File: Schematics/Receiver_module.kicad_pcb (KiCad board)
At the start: 2 copper layers, 54.6 x 44.5 mm, 17 parts, among them J1 I2C_ToTagger, T1 BC237, T2 BC237, T3 BC237

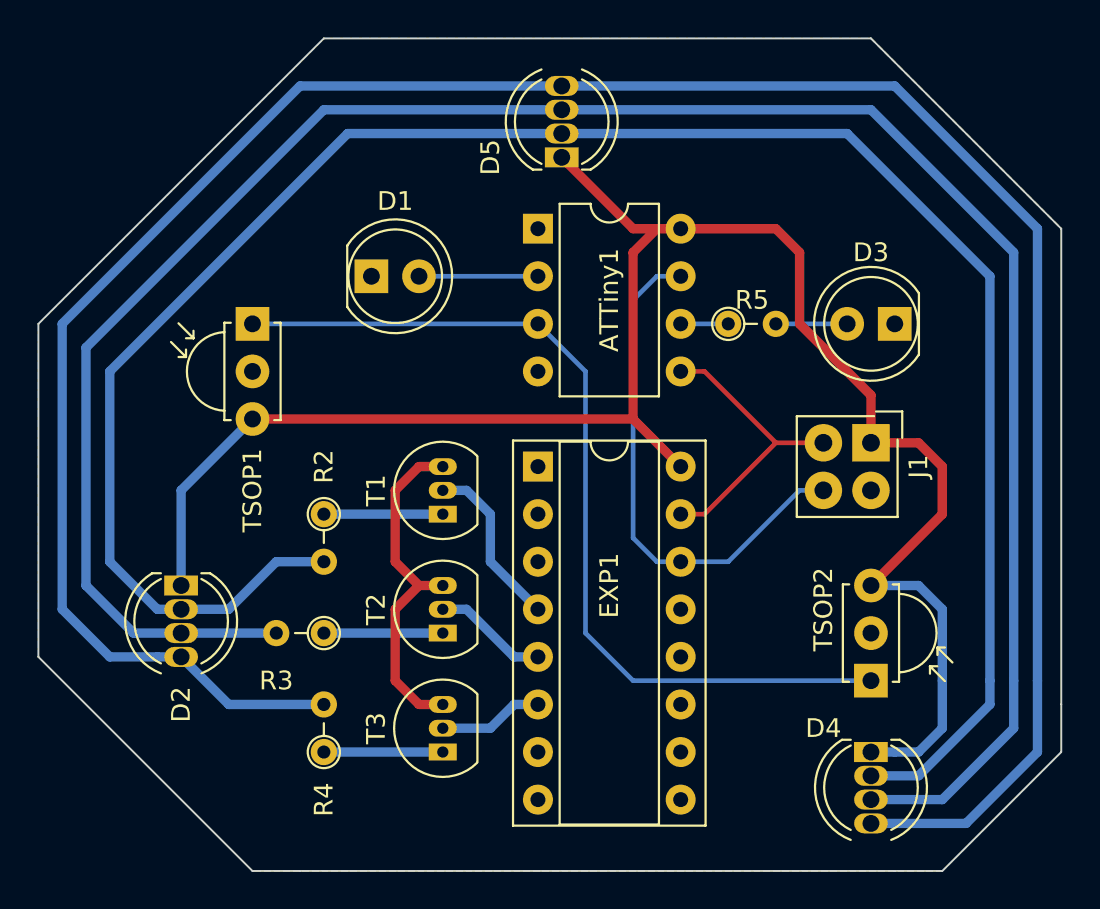
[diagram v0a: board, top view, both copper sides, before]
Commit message: New Version of Tagger/Receiver Schematics and PCBs
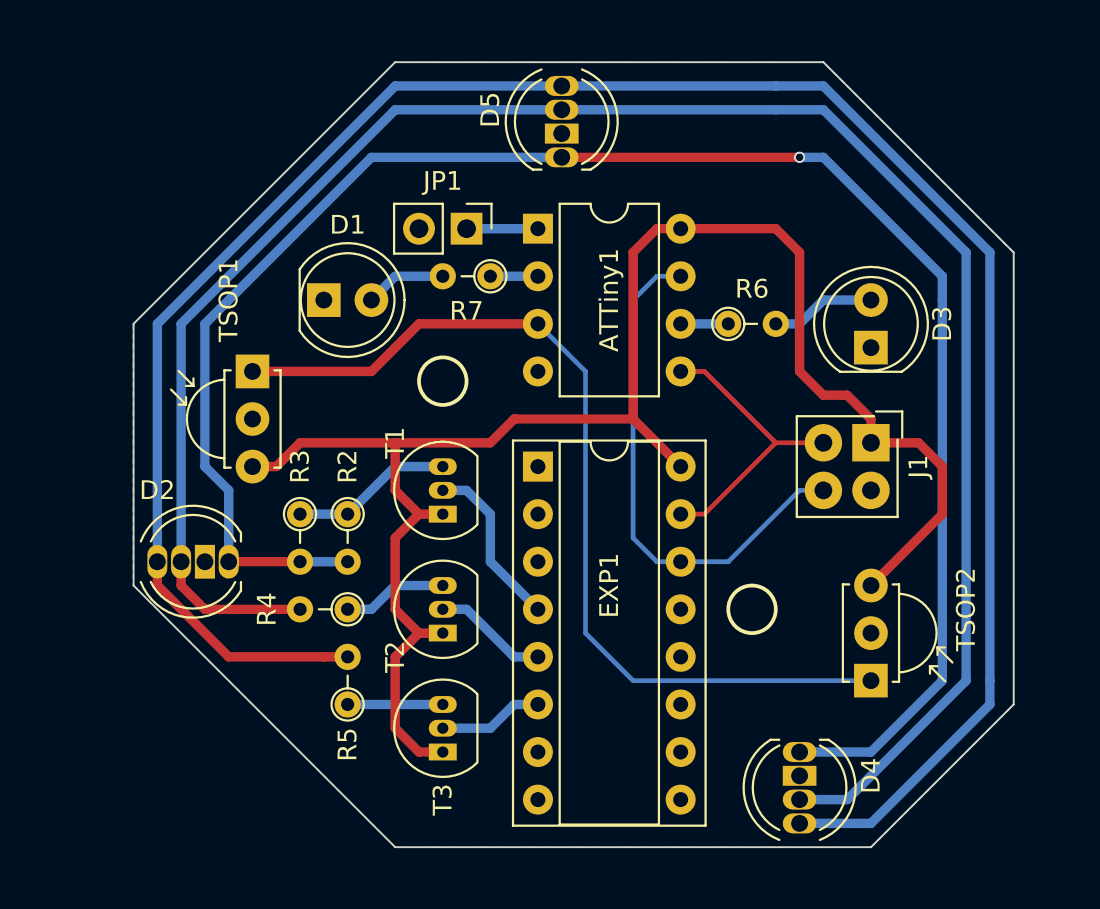
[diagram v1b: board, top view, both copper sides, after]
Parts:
- added JP1: Jumper_NO_Small, Pin_Headers:Pin_Header_Straight_1x02_Pitch2.54mm, F.Cu at (99.1, 94.0)
- added R6: R6, Resistors_THT:R_Axial_DIN0204_L3.6mm_D1.6mm_P2.54mm_Vertical, F.Cu at (113.0, 99.1)
- added R7: R, Resistors_THT:R_Axial_DIN0204_L3.6mm_D1.6mm_P2.54mm_Vertical, F.Cu at (100.3, 96.5)
- D2, D4, D5: value LED_ARGB -> LED_CRGB; footprint LEDs:LED_D5.0mm-4 -> RGB_LED_CC_5mm:LED_D5.0mm-4
- R2: value R2 -> 150R
- R3: value R3 -> 150R
- R4: value R4 -> 1k5
- R5: value R5 -> 1k
- moved R5 28.7 mm to (92.7, 119.4), turned to 90 degrees
- moved R4 7.73 mm to (92.7, 114.3), turned to 180 degrees
- moved R3 6.48 mm to (90.2, 109.2), turned to 270 degrees
- moved D4 3.81 mm to (116.8, 121.9)
- moved D1 2.84 mm to (91.4, 97.8)
- moved D2 2.84 mm to (86.4, 111.8), turned to 180 degrees
- moved TSOP1 2.54 mm to (87.6, 101.6)
- moved D3 1.80 mm to (120.7, 100.3), turned to 90 degrees
- moved R2 1.27 mm to (92.7, 109.2)
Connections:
- D1 pad 2: Net-(ATTiny1-Pad2) -> Net-(D1-Pad2)
- D2 pad 1: +5V -> GND
- D4 pad 1: +5V -> GND
- D5 pad 1: +5V -> GND
- R3 pad 1: Net-(R3-Pad1) -> Net-(R2-Pad1)
- R3 pad 2: Net-(D2-Pad3) -> Net-(D2-Pad2)
- R4 pad 2: Net-(D2-Pad4) -> Net-(D2-Pad3)
- R5 pad 1: Net-(ATTiny1-Pad6) -> Net-(R5-Pad1)
- R5 pad 2: Net-(D3-Pad2) -> Net-(D2-Pad4)
- T1 pad 1: Net-(R2-Pad1) -> +5V
- T1 pad 3: GND -> Net-(R2-Pad1)
- T2 pad 1: Net-(R3-Pad1) -> +5V
- T2 pad 3: GND -> Net-(R4-Pad1)
- T3 pad 1: Net-(R4-Pad1) -> +5V
- T3 pad 3: GND -> Net-(R5-Pad1)
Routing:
- net GND: track 18.6 -> 0.00 mm
- net Net-(D2-Pad4): track 130.2 -> 116.0 mm
- net Net-(D2-Pad2): track 109.9 -> 96.0 mm, vias 0 -> 1
- net Net-(D2-Pad3): track 116.5 -> 105.0 mm, vias 1 -> 0
- net +5V: track 98.9 -> 91.5 mm
- net Net-(R3-Pad1): track 6.35 -> 0.00 mm
- net Net-(R5-Pad1): track 0.00 -> 5.08 mm
- net Net-(D1-Pad2): track 0.00 -> 4.34 mm
- net Net-(ATTiny1-Pad2): track 6.35 -> 2.54 mm
- net Net-(ATTiny1-Pad1): track 0.00 -> 3.81 mm
- net Net-(R2-Pad1): track 6.35 -> 8.67 mm
- net Net-(D3-Pad2): track 3.81 -> 5.61 mm
- net Net-(ATTiny1-Pad3): track 49.1 -> 50.1 mm
- net Net-(R4-Pad1): track 6.35 -> 5.61 mm
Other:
- board size 54.6 x 44.5 mm -> 47 x 41.9 mm
